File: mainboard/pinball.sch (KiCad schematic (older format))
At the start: 20 parts

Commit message: Start on PCB layout
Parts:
- removed C? (x2): 22pF, symbol C
- removed D? (x4): D_Schottky, symbol D_Schottky
- removed J?: ScoreServo1, symbol CONN_01X02
- removed J?: ScoreServo2, symbol CONN_01X02
- removed J?: ScoreServo3, symbol CONN_01X02
- removed J?: ScoreServo4, symbol CONN_01X02
- removed Q? (x4): Q_NMOS_DGS, symbol Q_NMOS_DGS
- removed U?: ATMEGA328-AU, TQFP32, symbol ATMEGA328-AU
- removed Y?: Crystal, symbol Crystal
- added C3, C4: 22pF, Capacitors_SMD:C_0603, symbol C
- added CON1: AVR-ISP-6, Pin_Headers:Pin_Header_Straight_2x03, symbol AVR-ISP-6
- added D1, D2, D3, D4: D_Schottky, Diodes_SMD:SOD-323, symbol D_Schottky
- added IC1: ATMEGA328-A, Housings_QFP:TQFP-32_7x7mm_Pitch0.8mm, symbol ATMEGA328-A
- added P1, P2, P3, P4: SCREW_PLACEHOLDER, Mounting_Holes:MountingHole_3.2mm_M3_DIN965_Pad, symbol CONN_01X01
- added P5: PWR, Terminal_Blocks:TerminalBlock_Pheonix_MKDS1.5-4pol, symbol CONN_01X04
- added P6: SCORE_CONN, Terminal_Blocks:TerminalBlock_Pheonix_PT-3.5mm_16pol, symbol CONN_01X16
- added P7: CONN_02X24, Pin_Headers:Pin_Header_Straight_2x24, symbol CONN_02X24
- added Q1, Q3, Q5, Q7: Q_NMOS_GDS, TO_SOT_Packages_THT:TO-220_Neutral123_Vertical, symbol Q_NMOS_GDS
- added Q2, Q4, Q6, Q8: Q_NPN_BEC, TO_SOT_Packages_SMD:SOT-23, symbol Q_NPN_BEC
- added R1, R2, R3, R4: 1k, Resistors_SMD:R_1206, symbol R
- added W1, W2, W3: TEST_1P, Measurement_Points:Measurement_Point_Round-SMD-Pad_Big, symbol TEST_1P
- added Y1: Crystal, Crystals:Crystal_HC49-SD_SMD, symbol Crystal
- C1, C2: renamed from C?; footprint (none) -> Capacitors_SMD:C_0603
- U1: renamed from U?; value R-78E-1.0 -> R-78B5.0-2.0; footprint (none) -> Power_Integrations:TO-220; Digikey # 945-2201-ND -> 945-3042-ND
- U2: renamed from U?; footprint (none) -> teensy:Teensy35_36; symbol Teensy3.2 -> Teensy3.5
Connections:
- net labels added: CS0, CS1, CS2, CS3, CS4, CS5, MISO, MISO_AVR, MOSI, MOSI_AVR, NEOPIXEL, RST, SCK_AVR, SCLK, SCORE1, SCORE2, SCORE3, SCORE4, SCORE_OUT1, SCORE_OUT2, SCORE_OUT3, SCORE_OUT4, SCORE_ZERO1, SCORE_ZERO2, SCORE_ZERO3, SCORE_ZERO4, SCORE_ZERO_IN1, SCORE_ZERO_IN2, SCORE_ZERO_IN3, SCORE_ZERO_IN4, SWITCH1, SWITCH10, SWITCH11, SWITCH12, SWITCH13, SWITCH14, SWITCH15, SWITCH16, SWITCH17, SWITCH18, SWITCH19, SWITCH2, SWITCH20, SWITCH21, SWITCH22, SWITCH23, SWITCH24, SWITCH3, SWITCH4, SWITCH5, SWITCH6, SWITCH7, SWITCH8, SWITCH9, SWTICH8
- net labels removed: SERVO1, SERVO2, SERVO3, SERVO4
- wire segments 57 -> 179
- no-connect marks 0 -> 1

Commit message: KiCad 5.0 conversion. Start on slimming PCB.
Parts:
- removed D2, D3, D4: D_Schottky, Diodes_SMD:SOD-323, symbol D_Schottky
- removed P1, P2, P3: SCREW_PLACEHOLDER, Mounting_Holes:MountingHole_3.2mm_M3_DIN965_Pad, symbol CONN_01X01
- removed P6: SCORE_CONN, Terminal_Blocks:TerminalBlock_Pheonix_PT-3.5mm_16pol, symbol CONN_01X16
- removed Q3, Q5, Q7: Q_NMOS_GDS, TO_SOT_Packages_THT:TO-220_Neutral123_Vertical, symbol Q_NMOS_GDS
- removed U1: R-78B5.0-2.0, Power_Integrations:TO-220, symbol 7805
- added D2, D3, D4: D_Schottky, Diodes_SMD:SOD-323, symbol pinball-rescue:D_Schottky
- added J1: Conn_01x12, Pin_Headers:Pin_Header_Straight_2x06, symbol Connector_Generic:Conn_01x12
- added P1, P2, P3: SCREW_PLACEHOLDER, Mounting_Holes:MountingHole_3.2mm_M3_DIN965_Pad, symbol pinball-rescue:CONN_01X01
- added P8: Flipper Relay, Connect:PINHEAD1-2, symbol pinball-rescue:CONN_01X02
- added Q3, Q5, Q7: Q_NMOS_GDS, TO_SOT_Packages_THT:TO-220_Neutral123_Vertical, symbol pinball-rescue:Q_NMOS_GDS
- added U1: R-78B5.0-2.0, Power_Integrations:TO-220, symbol Regulator_Linear:L7805
- C1, C2, C3, C4: symbol C -> pinball-rescue:C
- CON1: symbol AVR-ISP-6 -> pinball-rescue:AVR-ISP-6
- D1: symbol D_Schottky -> pinball-rescue:D_Schottky
- IC1: symbol ATMEGA328-A -> pinball-rescue:ATMEGA328-A
- P4: symbol CONN_01X01 -> pinball-rescue:CONN_01X01
- P5: symbol CONN_01X04 -> pinball-rescue:CONN_01X04
- P7: symbol CONN_02X24 -> pinball-rescue:CONN_02X24
- Q1: footprint TO_SOT_Packages_THT:TO-220_Neutral123_Vertical -> Power_Integrations:TO-220; symbol Q_NMOS_GDS -> pinball-rescue:Q_NMOS_GDS
- Q2, Q4, Q6, Q8: symbol Q_NPN_BEC -> pinball-rescue:Q_NPN_BEC
- R1, R2, R3, R4: symbol R -> pinball-rescue:R
- U2: symbol Teensy3.5 -> teensy:Teensy3.5
- W1, W2, W3: symbol TEST_1P -> pinball-rescue:TEST_1P
- Y1: symbol Crystal -> pinball-rescue:Crystal
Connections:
- net labels added: CS, FLIPPER_ON_RELAY, SCORE_OUT1A, SCORE_OUT1B, SCORE_OUT2A, SCORE_OUT2B, SCORE_OUT3A, SCORE_OUT3B, SCORE_OUT4A, SCORE_OUT4B
- net labels removed: CS2, CS3, CS4, SCORE_OUT1, SCORE_OUT2, SCORE_OUT3, SCORE_OUT4, SWTICH8
- wire segments 179 -> 213
- no-connect marks 1 -> 56

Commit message: Voltage dividers on switch pins
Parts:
- removed J1: Conn_01x12, Pin_Headers:Pin_Header_Straight_2x06, symbol Connector_Generic:Conn_01x12
- removed P8: Flipper Relay, Connect:PINHEAD1-2, symbol pinball-rescue:CONN_01X02
- removed Q2, Q4, Q6, Q8: Q_NPN_BEC, TO_SOT_Packages_SMD:SOT-23, symbol pinball-rescue:Q_NPN_BEC
- removed R1, R2, R3, R4: 1k, Resistors_SMD:R_1206, symbol pinball-rescue:R
- added J1: Conn_01x14, Pin_Headers:Pin_Header_Straight_2x07, symbol Connector_Generic:Conn_01x14
- added J2: Conn_01x02, Pin_Headers:Pin_Header_Straight_1x02, symbol Connector_Generic:Conn_01x02
- Q1: footprint Power_Integrations:TO-220 -> TO_SOT_Packages_THT:TO-220_Neutral123_Vertical
- U2: footprint teensy:Teensy35_36 -> teensy:Teensy35_36_edge; symbol teensy:Teensy3.5 -> pinball-rescue:Teensy3.5-teensy
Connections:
- net labels added: RX, SWITCH_LOW1, SWITCH_LOW10, SWITCH_LOW11, SWITCH_LOW12, SWITCH_LOW13, SWITCH_LOW14, SWITCH_LOW15, SWITCH_LOW16, SWITCH_LOW17, SWITCH_LOW18, SWITCH_LOW19, SWITCH_LOW2, SWITCH_LOW20, SWITCH_LOW21, SWITCH_LOW22, SWITCH_LOW23, SWITCH_LOW24, SWITCH_LOW3, SWITCH_LOW4, SWITCH_LOW5, SWITCH_LOW6, SWITCH_LOW7, SWITCH_LOW8, SWITCH_LOW9, TX
- net labels removed: SCORE_OUT1B, SCORE_OUT2B, SCORE_OUT3B, SCORE_OUT4B
- wire segments 213 -> 185
- no-connect marks 56 -> 54
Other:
- moved on the sheet: C3, C4, CON1, P1, P2, P3, P4, P7, W1, W2, W3, Y1

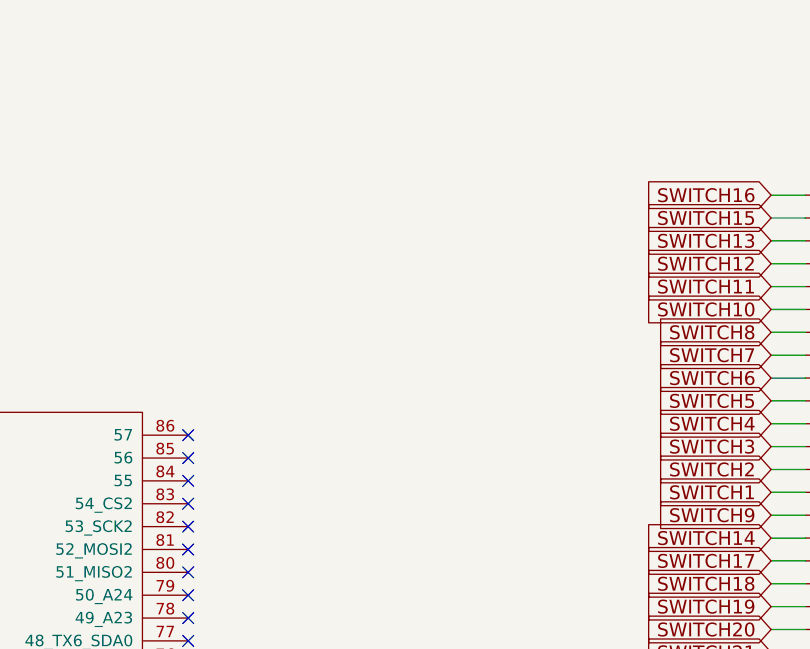
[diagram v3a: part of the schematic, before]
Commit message: Add power LED
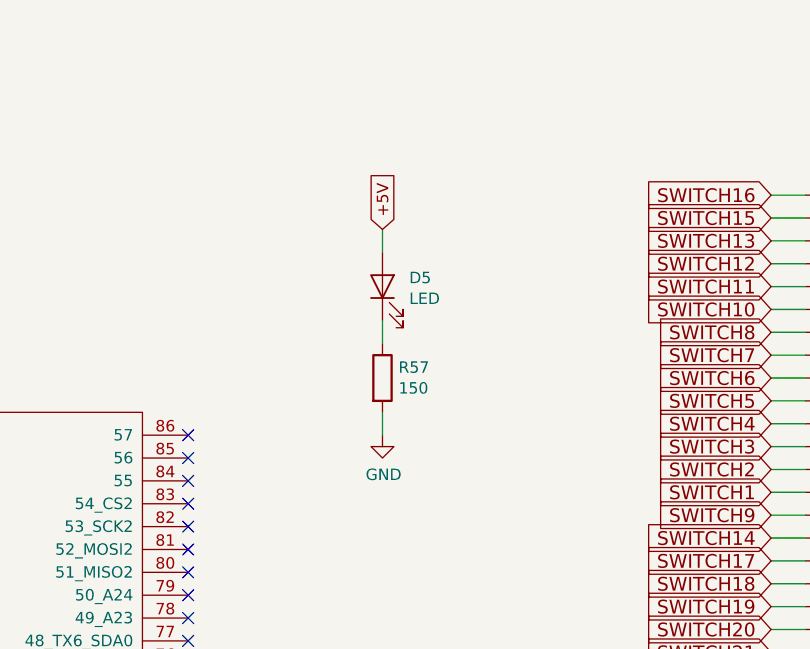
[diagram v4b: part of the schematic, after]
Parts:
- added D5: LED, LEDs:LED-0603, symbol Device:LED
- added R57: 150, Resistors_SMD:R_0603, symbol Device:R
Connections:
- net +5V: now also D5.2 (A)
- net GND: now also R57.2
- new net: D5.1 (K), R57.1
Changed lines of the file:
@@
 F1 "voltage_dividers.sch" 50
 $EndSheet
+$Comp
+L Device:LED D5
+U 1 1 5C5CDF26
+P 5050 1150
+F 0 "D5" V 5088 1033 50  0000 R CNN
+F 1 "LED" V 4997 1033 50  0000 R CNN
+F 2 "LEDs:LED-0603" H 5050 1150 50  0001 C CNN
+F 3 "~" H 5050 1150 50  0001 C CNN
+F 4 "160-1447-1-ND " V 5050 1150 50  0001 C CNN "Digikey #"
+	1    5050 1150
+	0    -1   -1   0
+$EndComp
+$Comp
+L Device:R R57
+U 1 1 5C5CE015
+P 5050 1550
+F 0 "R57" H 5120 1596 50  0000 L CNN
+F 1 "150" H 5120 1505 50  0000 L CNN
+F 2 "Resistors_SMD:R_0603" V 4980 1550 50  0001 C CNN
+F 3 "~" H 5050 1550 50  0001 C CNN
+F 4 "RNCP0603FTD150RCT-ND " H 5050 1550 50  0001 C CNN "Digikey #"
+	1    5050 1550
+	1    0    0    -1
+$EndComp
+$Comp
+L power:GND #PWR0104
+U 1 1 5C5CE094
+P 5050 1800
+F 0 "#PWR0104" H 5050 1550 50  0001 C CNN
+F 1 "GND" H 5055 1627 50  0000 C CNN
+F 2 "" H 5050 1800 50  0001 C CNN
+F 3 "" H 5050 1800 50  0001 C CNN
+	1    5050 1800
+	1    0    0    -1
+$EndComp
+Text GLabel 5050 900  1    50   Input ~ 0
++5V
+Wire Wire Line
+	5050 900  5050 1000
+Wire Wire Line
+	5050 1300 5050 1400
+Wire Wire Line
+	5050 1700 5050 1800
 $EndSCHEMATC

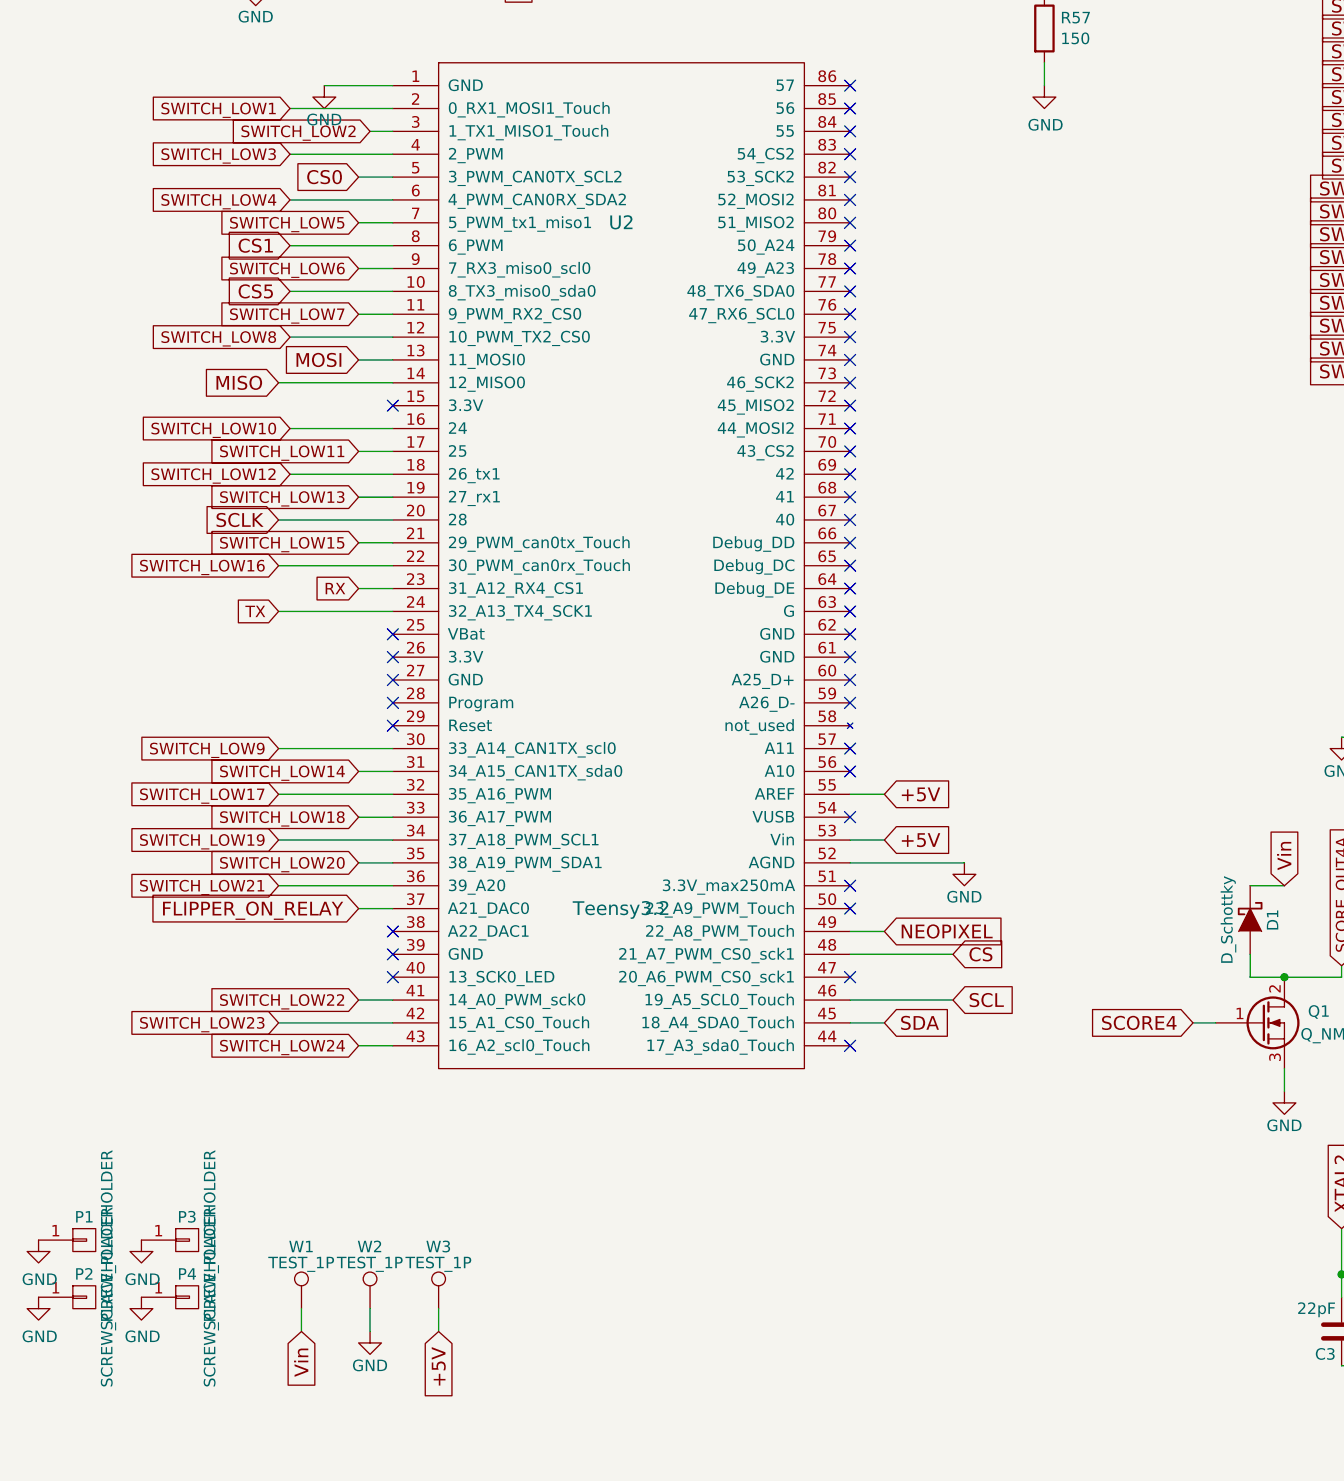
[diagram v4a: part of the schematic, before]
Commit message: Neopixel out. Lay out traces.
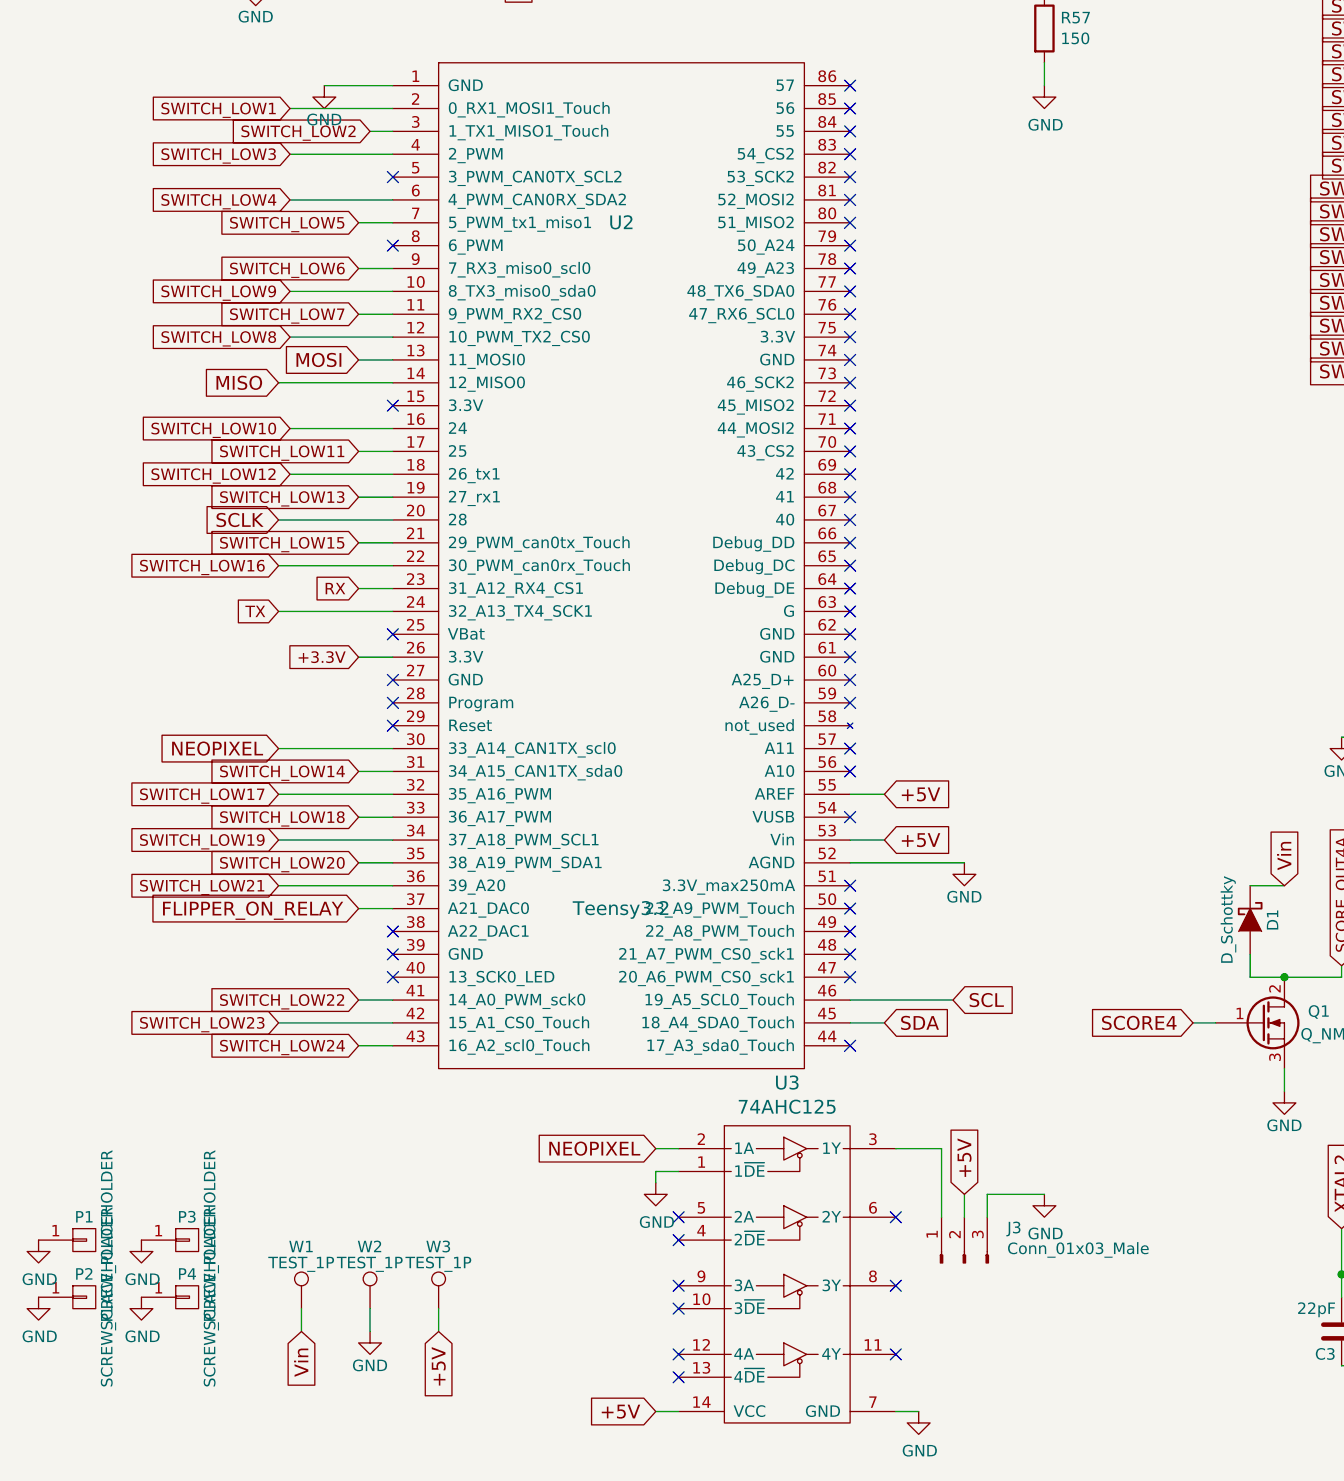
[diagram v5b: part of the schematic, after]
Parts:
- added J3: Conn_01x03_Male, Pin_Headers:Pin_Header_Straight_1x03, symbol Connector:Conn_01x03_Male
- added U3: 74AHC125, Housings_SSOP:TSSOP-14_4.4x5mm_Pitch0.65mm, symbol crumpschemes:74AHC125
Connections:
- net CS5 is gone; now on net SWITCH_LOW9: U2.10 (8_TX3_miso0_sda0)
- net +5V: now also J3.2 (Pin_2), U3.14 (VCC)
- net GND: now also J3.3 (Pin_3), U3.1 (1~DE), U3.7 (GND)
- net NEOPIXEL: now also U2.30 (33_A14_CAN1TX_scl0), U3.2 (1A); no longer U2.49 (22_A8_PWM_Touch)
- net SWITCH_LOW9: no longer U2.30 (33_A14_CAN1TX_scl0)
- net +3.3V: now reaches U2.26 (3.3V)
- net CS: no longer names the net of U2.48 (21_A7_PWM_CS0_sck1)
- net CS0: no longer names the net of U2.5 (3_PWM_CAN0TX_SCL2)
- net CS1: no longer names the net of U2.8 (6_PWM)
- new net: J3.1 (Pin_1), U3.3 (1Y)
- no-connect marks 54 -> 66
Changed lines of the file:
@@
 	1    0    0    -1
 $EndComp
-Text GLabel 1750 2500 0    60   Input ~ 0
-CS1
-Text GLabel 2050 2200 0    60   Input ~ 0
-CS0
-Wire Wire Line
-	2050 2200 2200 2200
-Wire Wire Line
-	2200 2500 1750 2500
-Text GLabel 4650 5600 2    60   Input ~ 0
-CS
-Wire Wire Line
-	4650 5600 4200 5600
-Text GLabel 1750 2700 0    60   Input ~ 0
-CS5
-Wire Wire Line
-	2200 2700 1750 2700
 $Comp
 L pinball-rescue:CONN_01X04 P5
@@
 Wire Wire Line
 	2400 7150 2400 7250
-Text GLabel 4350 5500 2    60   Input ~ 0
+Text GLabel 1700 4700 0    60   Input ~ 0
 NEOPIXEL
-Wire Wire Line
-	4350 5500 4200 5500
 Wire Wire Line
 	2050 6000 2200 6000
@@
 NoConn ~ 2200 5500
 NoConn ~ 2200 4200
-NoConn ~ 2200 4300
 NoConn ~ 2200 4400
 NoConn ~ 2200 4500
@@
 Text GLabel 1750 1900 0    50   Input ~ 0
 SWITCH_LOW1
-Text GLabel 1700 4700 0    50   Input ~ 0
+Text GLabel 1750 2700 0    50   Input ~ 0
 SWITCH_LOW9
 Text GLabel 2050 4800 0    50   Input ~ 0
@@
 Wire Wire Line
 	5050 1700 5050 1800
+$Comp
+L Connector:Conn_01x03_Male J3
+U 1 1 5C5D4D4A
+P 4700 6950
+F 0 "J3" V 4853 6763 50  0000 R CNN
+F 1 "Conn_01x03_Male" V 4762 6763 50  0000 R CNN
+F 2 "Pin_Headers:Pin_Header_Straight_1x03" H 4700 6950 50  0001 C CNN
+F 3 "~" H 4700 6950 50  0001 C CNN
+	1    4700 6950
+	0    -1   -1   0
+$EndComp
+Text GLabel 3350 6450 0    60   Input ~ 0
+NEOPIXEL
+$Comp
+L power:GND #PWR0106
+U 1 1 5C5D507A
+P 5050 6650
+F 0 "#PWR0106" H 5050 6400 50  0001 C CNN
+F 1 "GND" H 5055 6477 50  0000 C CNN
+F 2 "" H 5050 6650 50  0001 C CNN
+F 3 "" H 5050 6650 50  0001 C CNN
+	1    5050 6650
+	1    0    0    -1
+$EndComp
+Wire Wire Line
+	4800 6750 4800 6650
+Wire Wire Line
+	4800 6650 5050 6650
+Text GLabel 4700 6650 1    60   Input ~ 0
++5V
+Wire Wire Line
+	4700 6650 4700 6750
+Text GLabel 2050 4300 0    50   Input ~ 0
++3.3V
+Wire Wire Line
+	2050 4300 2200 4300
+$Comp
+L crumpschemes:74AHC125 U3
+U 1 1 5C6093D9
+P 3950 6950
+F 0 "U3" H 3925 7737 60  0000 C CNN
+F 1 "74AHC125" H 3925 7631 60  0000 C CNN
+F 2 "Housings_SSOP:TSSOP-14_4.4x5mm_Pitch0.65mm" H 3950 6950 60  0001 C CNN
+F 3 "" H 3950 6950 60  0001 C CNN
+F 4 "1727-6305-1-ND" H 3950 6950 50  0001 C CNN "Digikey #"
+	1    3950 6950
+	1    0    0    -1
+$EndComp
+Text GLabel 3350 7600 0    60   Input ~ 0
++5V
+$Comp
+L power:GND #PWR0107
+U 1 1 5C609626
+P 4500 7600
+F 0 "#PWR0107" H 4500 7350 50  0001 C CNN
+F 1 "GND" H 4505 7427 50  0000 C CNN
+F 2 "" H 4500 7600 50  0001 C CNN
+F 3 "" H 4500 7600 50  0001 C CNN
+	1    4500 7600
+	1    0    0    -1
+$EndComp
+$Comp
+L power:GND #PWR0108
+U 1 1 5C609753
+P 3350 6600
+F 0 "#PWR0108" H 3350 6350 50  0001 C CNN
+F 1 "GND" H 3355 6427 50  0000 C CNN
+F 2 "" H 3350 6600 50  0001 C CNN
+F 3 "" H 3350 6600 50  0001 C CNN
+	1    3350 6600
+	1    0    0    -1
+$EndComp
+Wire Wire Line
+	3450 6550 3350 6550
+Wire Wire Line
+	3350 6550 3350 6600
+Wire Wire Line
+	3350 6450 3450 6450
+Wire Wire Line
+	3350 7600 3450 7600
+NoConn ~ 3450 6750
+NoConn ~ 3450 6850
+NoConn ~ 3450 7050
+NoConn ~ 3450 7150
+NoConn ~ 3450 7350
+NoConn ~ 3450 7450
+NoConn ~ 4400 7350
+NoConn ~ 4400 7050
+NoConn ~ 4400 6750
+Wire Wire Line
+	4400 7600 4500 7600
+Wire Wire Line
+	4600 6750 4600 6450
+Wire Wire Line
+	4600 6450 4400 6450
+NoConn ~ 4200 5500
+NoConn ~ 4200 5600
+NoConn ~ 2200 2500
+Wire Wire Line
+	2200 2700 1750 2700
+NoConn ~ 2200 2200
 $EndSCHEMATC
